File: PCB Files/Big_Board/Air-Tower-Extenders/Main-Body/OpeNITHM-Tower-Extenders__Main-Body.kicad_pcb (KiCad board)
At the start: 2 copper layers, 29.9 x 34.6 mm, 6 parts, among them J1 Conn_01x04_Male, J2 Conn_01x04_Male, J3 Conn_01x09_Male, J4 Conn_01x09_Male

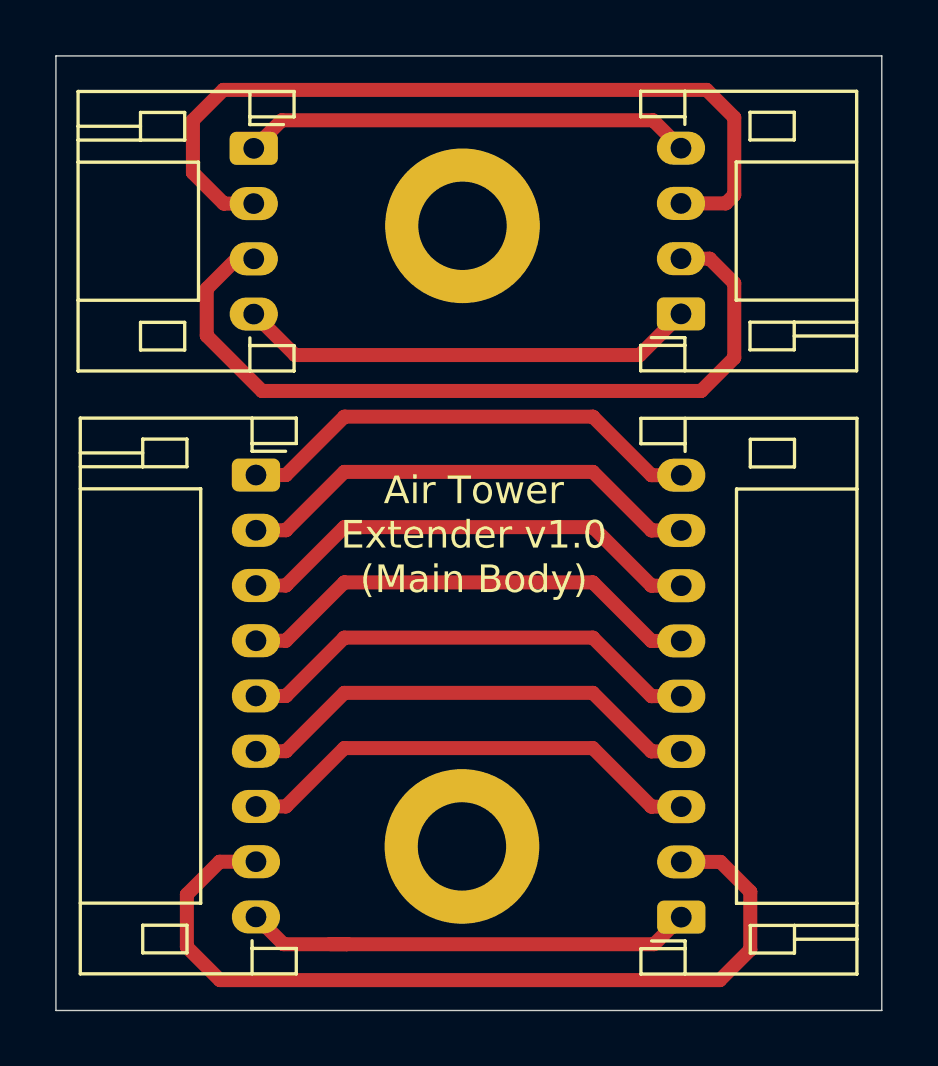
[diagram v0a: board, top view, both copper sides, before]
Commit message: Update the gerbers for the air extender PCBs
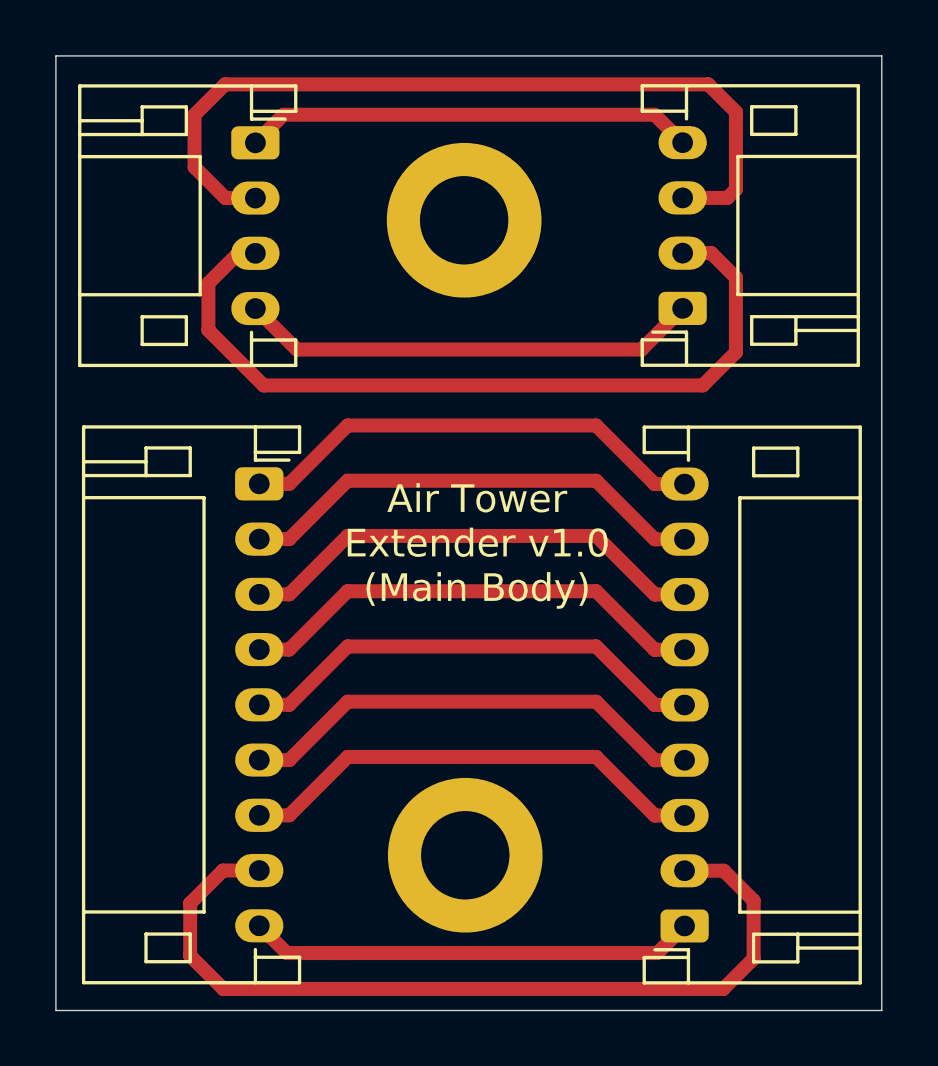
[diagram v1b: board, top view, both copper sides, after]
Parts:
- moved J3 0.34 mm to (66.9, 59.4)
- moved H2 0.34 mm to (74.4, 72.9)
- moved J4 0.34 mm to (82.3, 75.4)
- moved H1 0.21 mm to (74.3, 49.9)
- moved J1 0.21 mm to (66.8, 47.1)
- moved J2 0.21 mm to (82.2, 53.1)
